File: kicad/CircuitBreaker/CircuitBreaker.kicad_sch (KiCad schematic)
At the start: 59 parts, among them J1 PH2.54, J4 PH2.54, J5 downlink, J6 uplink, J7 PWN-In-5v, SW1 usbIAP, T1 CT104D, T2 CT104D, T3 CT104D, T4 CT104D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

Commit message: corrected stc tssop20
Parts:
- JP1, JP2: footprint Jumper:SolderJumper-3_P1.3mm_Bridged2Bar12_RoundedPad1.0x1.5mm_NumberLabels -> Jumper:SolderJumper-3_P1.3mm_Bridged12_RoundedPad1.0x1.5mm
- U2: footprint Package_SO:TSSOP-20_4.4x5mm_P0.4mm -> Package_SO:TSSOP-20_4.4x6.5mm_P0.65mm
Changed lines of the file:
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@@
     (property "Reference" "JP2" (id 0) (at 204.47 138.43 0))
     (property "Value" "bus-type" (id 1) (at 207.01 133.35 0))
-    (property "Footprint" "Jumper:SolderJumper-3_P1.3mm_Bridged2Bar12_RoundedPad1.0x1.5mm_NumberLabels" (id 2) (at 207.01 135.89 0)
+    (property "Footprint" "Jumper:SolderJumper-3_P1.3mm_Bridged12_RoundedPad1.0x1.5mm" (id 2) (at 207.01 135.89 0)
       (effects (font (size 1.27 1.27)) hide)
     )
@@
     (property "Reference" "U2" (id 0) (at 146.05 43.18 0))
     (property "Value" "STC8H8K64U" (id 1) (at 146.05 78.74 0))
-    (property "Footprint" "Package_SO:TSSOP-20_4.4x5mm_P0.4mm" (id 2) (at 139.7 64.77 0)
+    (property "Footprint" "Package_SO:TSSOP-20_4.4x6.5mm_P0.65mm" (id 2) (at 139.7 64.77 0)
       (effects (font (size 1.27 1.27)) hide)
     )
@@
     (property "Reference" "JP1" (id 0) (at 193.04 133.35 0))
     (property "Value" "bus-type" (id 1) (at 195.58 128.27 0))
-    (property "Footprint" "Jumper:SolderJumper-3_P1.3mm_Bridged2Bar12_RoundedPad1.0x1.5mm_NumberLabels" (id 2) (at 195.58 130.81 0)
+    (property "Footprint" "Jumper:SolderJumper-3_P1.3mm_Bridged12_RoundedPad1.0x1.5mm" (id 2) (at 195.58 130.81 0)
       (effects (font (size 1.27 1.27)) hide)
     )
@@
     )
     (path "/f6fabe2b-8561-4cc8-8c90-c9ae9db53609"
-      (reference "JP1") (unit 1) (value "bus-type") (footprint "Jumper:SolderJumper-3_P1.3mm_Bridged2Bar12_RoundedPad1.0x1.5mm_NumberLabels")
+      (reference "JP1") (unit 1) (value "bus-type") (footprint "Jumper:SolderJumper-3_P1.3mm_Bridged12_RoundedPad1.0x1.5mm")
     )
     (path "/41b2986c-a9b1-4077-a88d-a6bcda6ce253"
-      (reference "JP2") (unit 1) (value "bus-type") (footprint "Jumper:SolderJumper-3_P1.3mm_Bridged2Bar12_RoundedPad1.0x1.5mm_NumberLabels")
+      (reference "JP2") (unit 1) (value "bus-type") (footprint "Jumper:SolderJumper-3_P1.3mm_Bridged12_RoundedPad1.0x1.5mm")
     )
     (path "/095bcb87-9f60-42dc-b5fb-9fe5feadea0c"
@@
     )
     (path "/4a27f6f5-b0e4-4aa4-a25b-c8f6fbf1beb6"
-      (reference "U2") (unit 1) (value "STC8H8K64U") (footprint "Package_SO:TSSOP-20_4.4x5mm_P0.4mm")
+      (reference "U2") (unit 1) (value "STC8H8K64U") (footprint "Package_SO:TSSOP-20_4.4x6.5mm_P0.65mm")
     )
     (path "/06ee62ce-0f50-4fac-8235-fc1e35a64b1b"

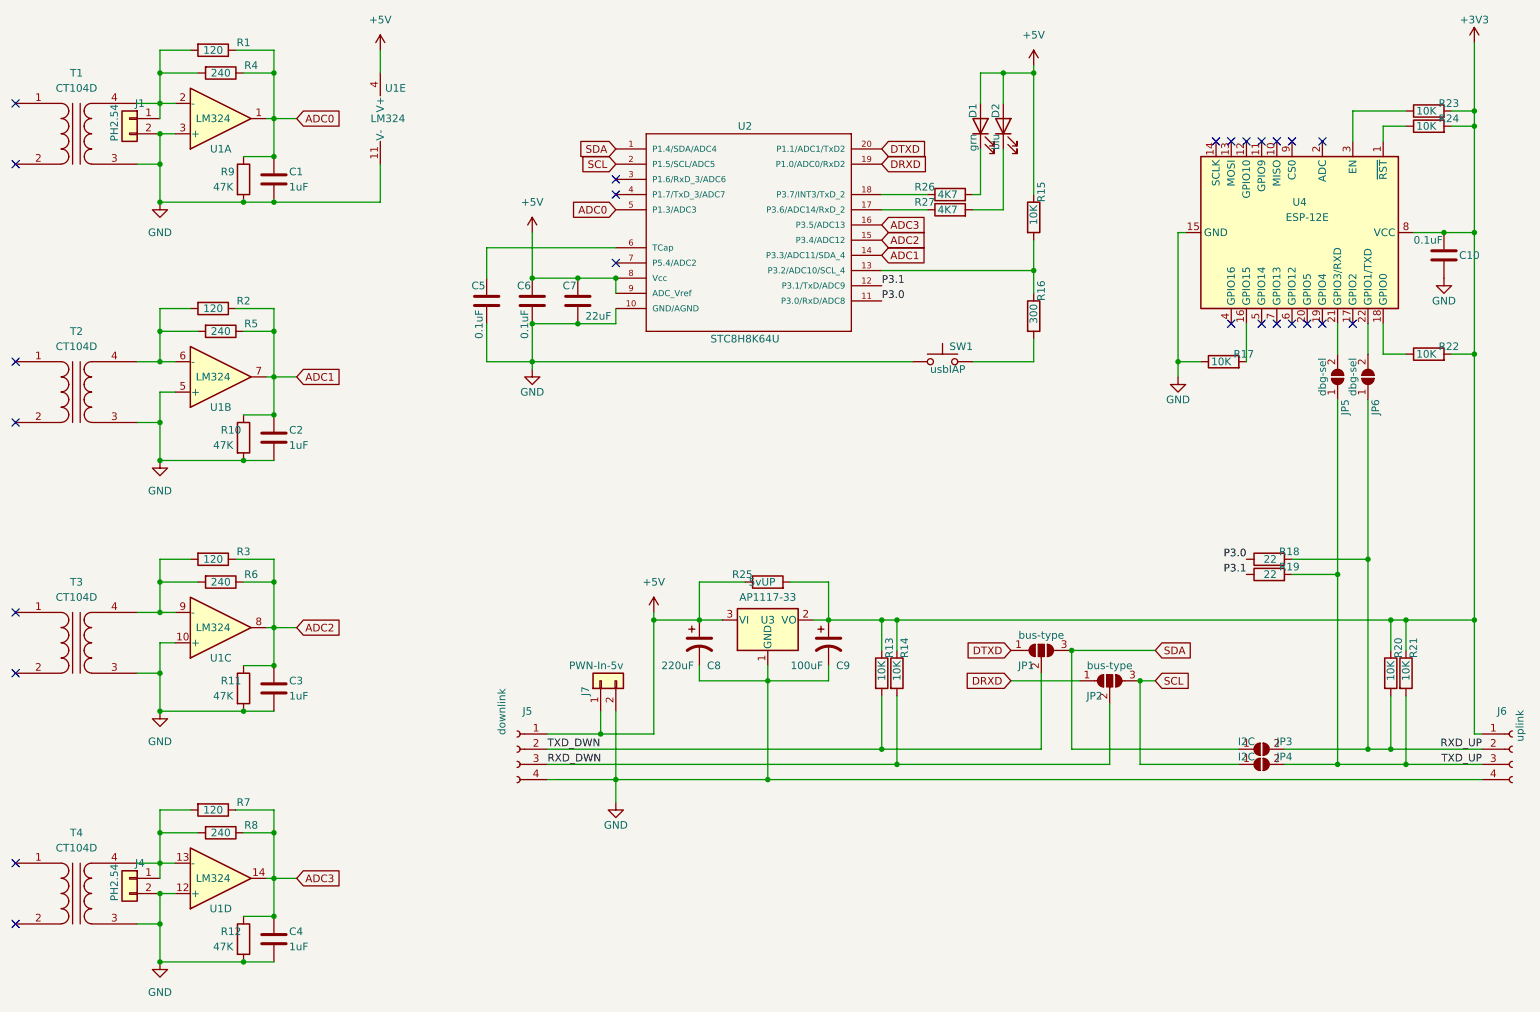
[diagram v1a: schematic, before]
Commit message: cm104 add jack
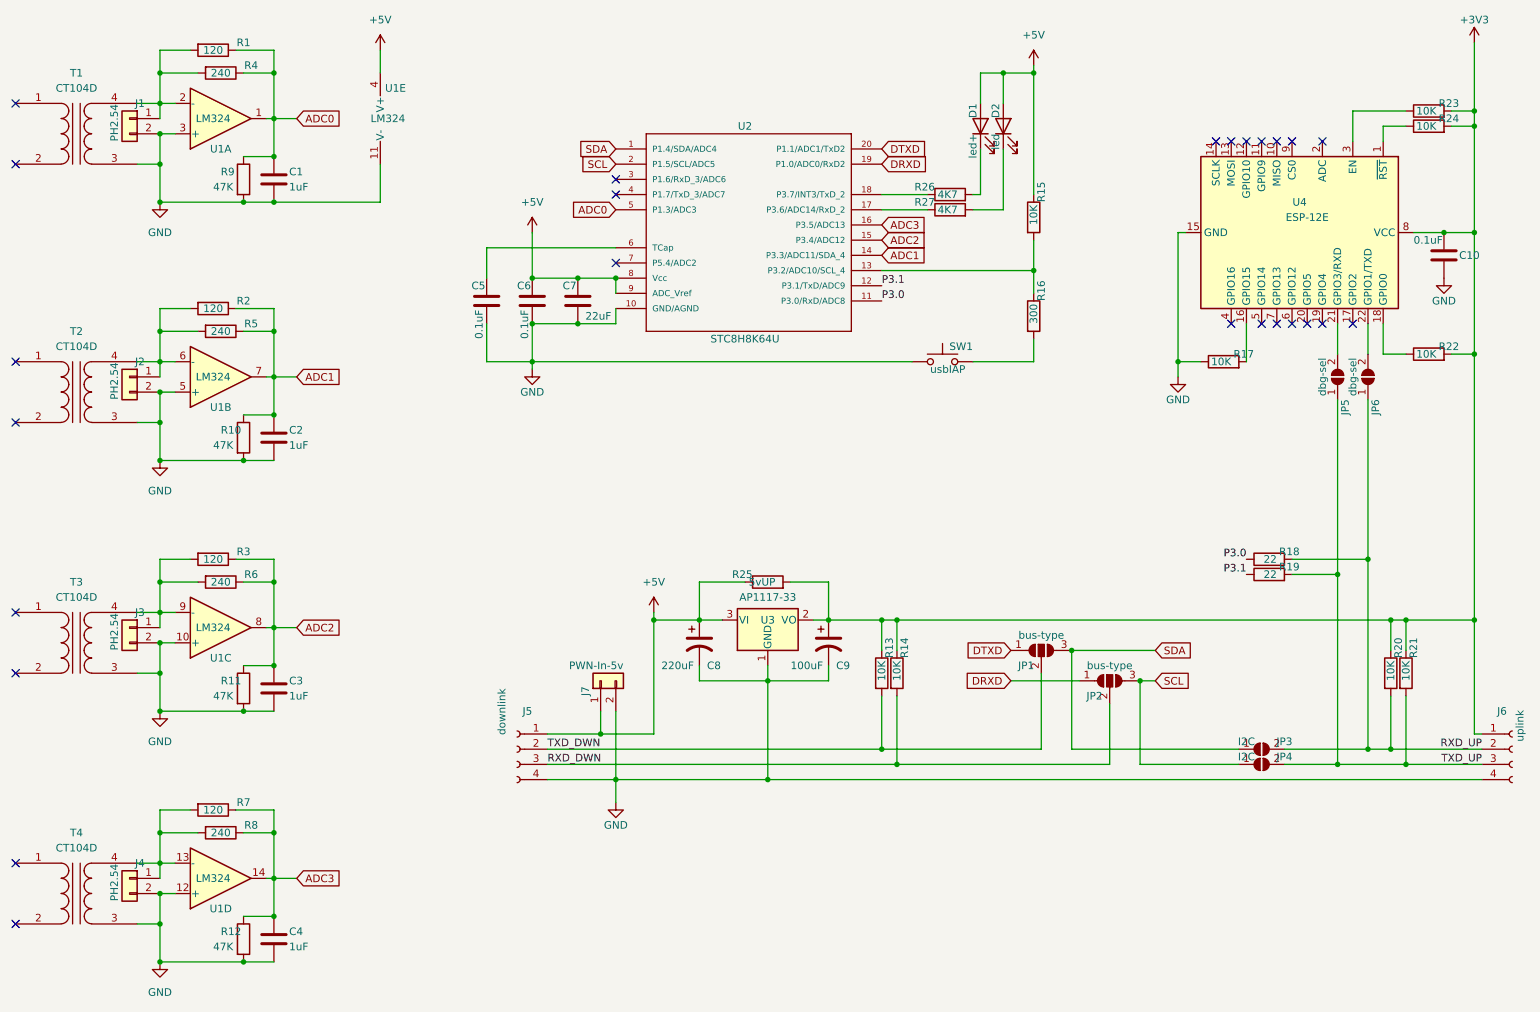
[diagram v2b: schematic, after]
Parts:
- added J2, J3: PH2.54, Connector_PinHeader_2.54mm:PinHeader_1x02_P2.54mm_Vertical, symbol Connector_Generic:Conn_01x02
- D1: value grn -> led+
- D2: value blu -> led
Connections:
- net GND: now also J2.2 (Pin_2), J3.2 (Pin_2)
- net at R3.2, R6.2, T3.4 (SB)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: now also J3.1 (Pin_1)
- net at R2.2, R5.2, T2.4 (SB)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: now also J2.1 (Pin_1)
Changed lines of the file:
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@@
   (junction (at 256.54 125.73) (diameter 0) (color 0 0 0 0)
   )
+  (junction (at 48.26 87.63) (diameter 0) (color 0 0 0 0)
+  )
   (junction (at 118.11 68.58) (diameter 0) (color 0 0 0 0)
   )
@@
   )
   (junction (at 218.44 82.55) (diameter 0) (color 0 0 0 0)
+  )
+  (junction (at 48.26 129.54) (diameter 0) (color 0 0 0 0)
   )
   (junction (at 67.31 91.44) (diameter 0) (color 0 0 0 0)
@@
     (stroke (width 0) (type default) (color 0 0 0 0))
   )
+  (wire (pts (xy 48.26 124.46) (xy 48.26 127))
+    (stroke (width 0) (type default) (color 0 0 0 0))
+  )
   (wire (pts (xy 102.87 82.55) (xy 110.49 82.55))
     (stroke (width 0) (type default) (color 0 0 0 0))
@@
   )
   (wire (pts (xy 67.31 115.57) (xy 67.31 119.38))
+    (stroke (width 0) (type default) (color 0 0 0 0))
+  )
+  (wire (pts (xy 48.26 82.55) (xy 48.26 85.09))
     (stroke (width 0) (type default) (color 0 0 0 0))
   )
@@
     )
     (property "Datasheet" "~" (id 3) (at 57.15 157.48 0)
+      (effects (font (size 1.27 1.27)) hide)
+    )
+    (pin "1")
+    (pin "2")
+  )
+  (symbol (lib_id "Connector_Generic:Conn_01x02") (at 43.18 127 0) (mirror y) (unit 1)
+    (in_bom yes) (on_board yes)
+    (property "Reference" "J3" (id 0) (at 45.72 124.46 0)
+      (effects (font (size 1.27 1.27)) (justify left))
+    )
+    (property "Value" "PH2.54" (id 1) (at 40.64 130.81 90)
+      (effects (font (size 1.27 1.27)) (justify left))
+    )
+    (property "Footprint" "Connector_PinHeader_2.54mm:PinHeader_1x02_P2.54mm_Vertical" (id 2) (at 43.18 127 0)
+      (effects (font (size 1.27 1.27)) hide)
+    )
+    (property "Datasheet" "~" (id 3) (at 43.18 127 0)
       (effects (font (size 1.27 1.27)) hide)
     )
@@
       (effects (font (size 1.27 1.27)) (justify right))
     )
-    (property "Value" "blu" (id 1) (at 187.96 44.45 0)
+    (property "Value" "led" (id 1) (at 187.96 44.45 0)
       (effects (font (size 1.27 1.27)) (justify right))
     )
@@
       (effects (font (size 1.27 1.27)) (justify right))
     )
-    (property "Value" "grn" (id 1) (at 184.15 44.45 0)
+    (property "Value" "led+" (id 1) (at 184.15 44.45 0)
       (effects (font (size 1.27 1.27)) (justify right))
     )
@@
     (pin "2")
   )
+  (symbol (lib_id "Connector_Generic:Conn_01x02") (at 43.18 85.09 0) (mirror y) (unit 1)
+    (in_bom yes) (on_board yes)
+    (property "Reference" "J2" (id 0) (at 45.72 82.55 0)
+      (effects (font (size 1.27 1.27)) (justify left))
+    )
+    (property "Value" "PH2.54" (id 1) (at 40.64 88.9 90)
+      (effects (font (size 1.27 1.27)) (justify left))
+    )
+    (property "Footprint" "Connector_PinHeader_2.54mm:PinHeader_1x02_P2.54mm_Vertical" (id 2) (at 43.18 85.09 0)
+      (effects (font (size 1.27 1.27)) hide)
+    )
+    (property "Datasheet" "~" (id 3) (at 43.18 85.09 0)
+      (effects (font (size 1.27 1.27)) hide)
+    )
+    (pin "1")
+    (pin "2")
+  )
   (symbol (lib_id "Jumper:SolderJumper_3_Open") (at 195.58 130.81 0) (unit 1)
     (in_bom yes) (on_board yes)
@@
     )
     (path "/5043d550-329f-4c22-af2e-a891b18ddb8a"
-      (reference "D1") (unit 1) (value "grn") (footprint "LED_SMD:LED_0603_1608Metric")
+      (reference "D1") (unit 1) (value "led+") (footprint "LED_SMD:LED_0603_1608Metric")
     )
     (path "/222a9ad1-ac03-480c-938b-316b28742e5a"
-      (reference "D2") (unit 1) (value "blu") (footprint "LED_SMD:LED_0603_1608Metric")
+      (reference "D2") (unit 1) (value "led") (footprint "LED_SMD:LED_0603_1608Metric")
     )
     (path "/ed5e7f7b-7ab0-466d-9f53-71c8cd09f405"
       (reference "J1") (unit 1) (value "PH2.54") (footprint "Connector_PinHeader_2.54mm:PinHeader_1x02_P2.54mm_Vertical")
     )
+    (path "/f5354c1d-8f43-4b8e-82e1-092763d99e98"
+      (reference "J2") (unit 1) (value "PH2.54") (footprint "Connector_PinHeader_2.54mm:PinHeader_1x02_P2.54mm_Vertical")
+    )
+    (path "/0626044b-52d2-4454-842b-65a91de652dd"
+      (reference "J3") (unit 1) (value "PH2.54") (footprint "Connector_PinHeader_2.54mm:PinHeader_1x02_P2.54mm_Vertical")
+    )
     (path "/193502b3-a5e3-46c9-a7b1-77019833c298"
